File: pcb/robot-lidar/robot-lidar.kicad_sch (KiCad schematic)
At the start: 53 parts, among them J10 Conn_01x18, J11 USB_A, J2 YLIDAR X4, J3 Jack-DC, J5 Conn_01x02, J5 Conn_02x03_Odd_Even, J6 Conn_01x02, J7 Conn_01x02, J7 Conn_ARM_SWD_TagConnect_TC2030, J8 Conn_01x02, J9 Conn_01x18, SW1 SW_SPST, U1 STM32F429VETx, U2 LM317-3.3_SOT-223, U2 MPU-6050, U4 MX1508, U5 MX1508, Y1 Crystal

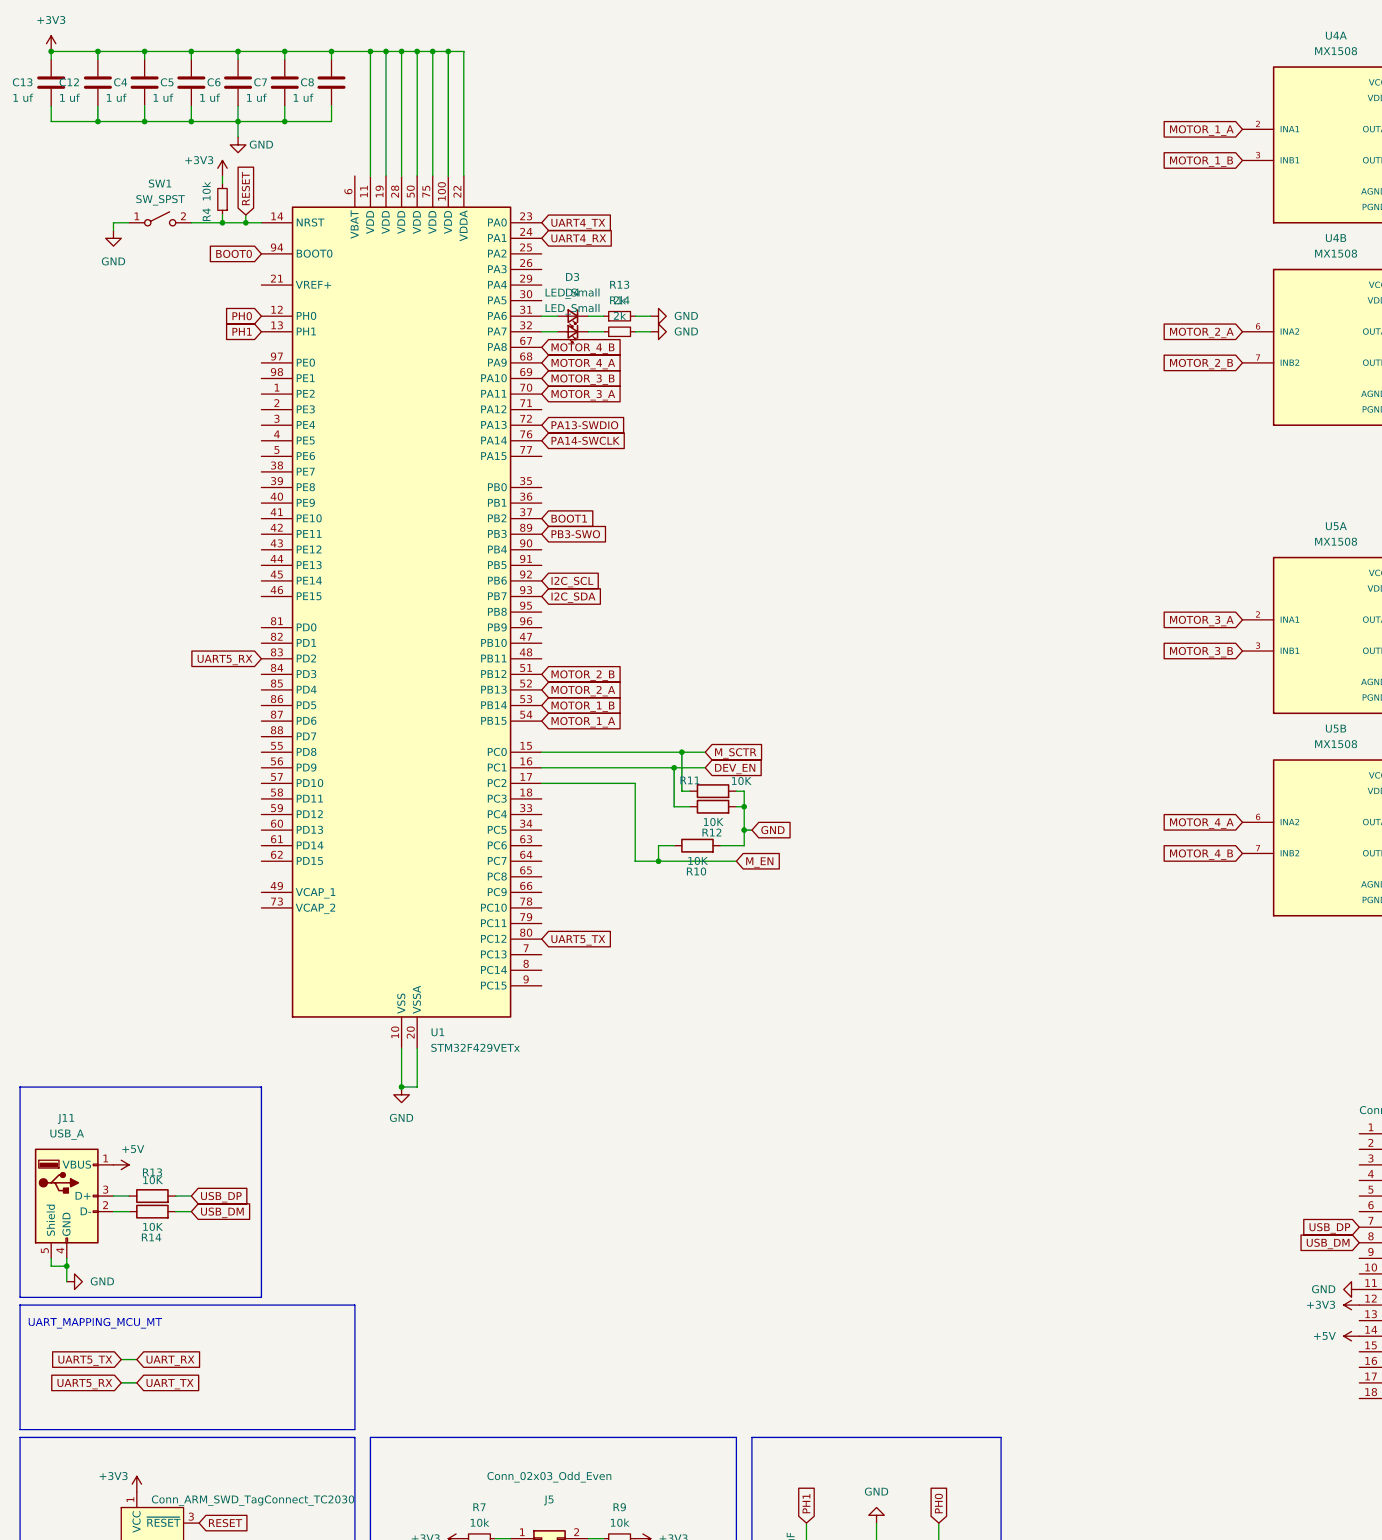
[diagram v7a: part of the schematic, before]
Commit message: stm32f4 to stm32f1 + linkit to raspberry
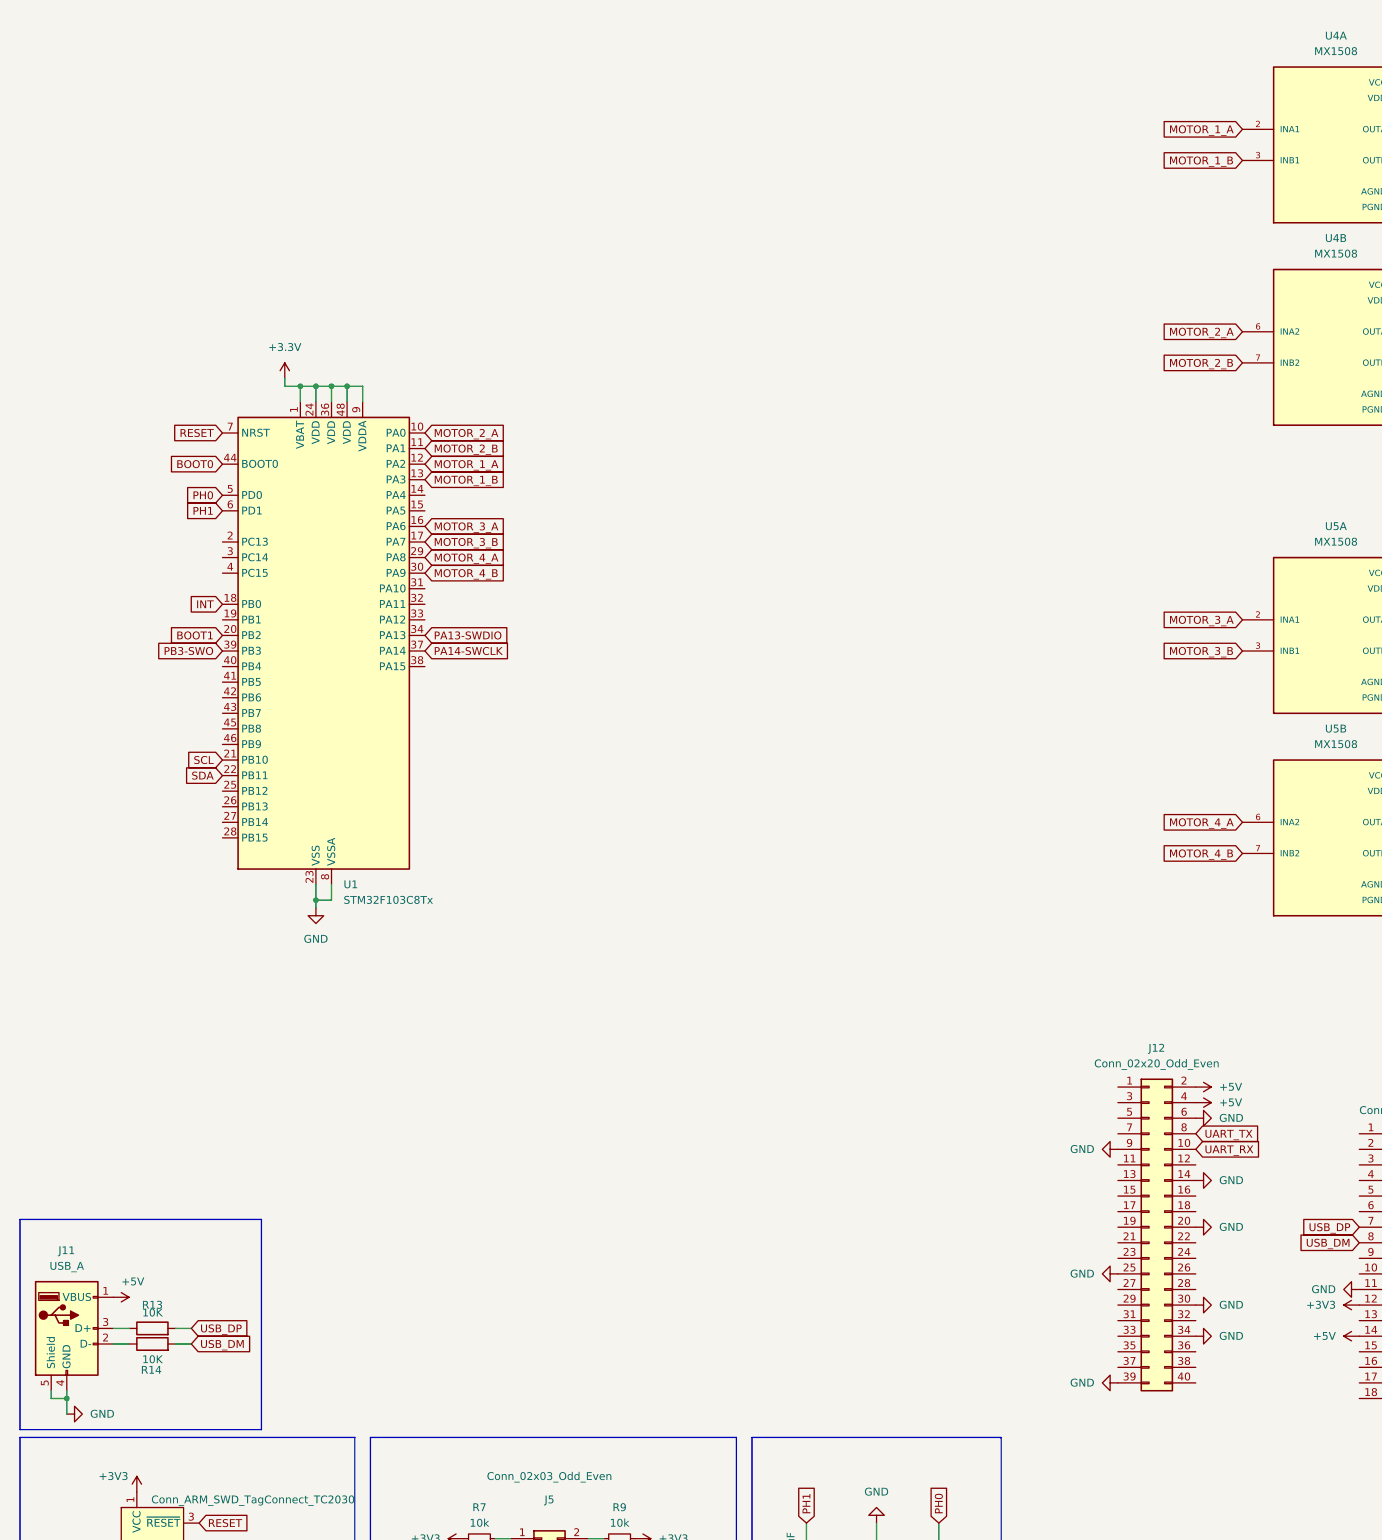
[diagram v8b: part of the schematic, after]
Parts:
- removed C12, C13, C4, C5, C6, C7, C8: 1 uf, Capacitor_SMD:C_0603_1608Metric, symbol Device:C
- removed D3, D4: LED_Small, Resistor_SMD:R_0603_1608Metric, symbol Device:LED_Small
- removed R10, R11, R12: 10K, Resistor_SMD:R_0603_1608Metric, symbol Device:R
- removed R13, R14: 2k, Resistor_SMD:R_0603_1608Metric, symbol Device:R_Small
- removed R4: 10k, Resistor_SMD:R_0603_1608Metric, symbol Device:R_Small
- removed SW1: SW_SPST, Button_Switch_SMD:SW_SPST_CK_RS282G05A3, symbol Switch:SW_SPST
- removed U1: STM32F429VETx, Package_QFP:LQFP-100_14x14mm_P0.5mm, symbol MCU_ST_STM32F4:STM32F429VETx
- added J12: Conn_02x20_Odd_Even, symbol Connector_Generic:Conn_02x20_Odd_Even
- added U1: STM32F103C8Tx, Package_QFP:LQFP-48_7x7mm_P0.5mm, symbol MCU_ST_STM32F1:STM32F103C8Tx
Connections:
- net +5V: now also J12.2 (Pin_2), J12.4 (Pin_4)
- net BOOT0: now also U1.44 (BOOT0)
- net BOOT1: now also U1.20 (PB2)
- net GND: now also J12.14 (Pin_14), J12.20 (Pin_20), J12.25 (Pin_25), J12.30 (Pin_30), J12.34 (Pin_34), J12.39 (Pin_39), J12.6 (Pin_6), J12.9 (Pin_9), U1.23 (VSS), U1.35 (VSS), U1.47 (VSS), U1.8 (VSSA)
- net MOTOR_1_A: now also U1.12 (PA2)
- net MOTOR_1_B: now also U1.13 (PA3)
- net MOTOR_2_A: now also U1.10 (PA0)
- net MOTOR_2_B: now also U1.11 (PA1)
- net MOTOR_3_A: now also U1.16 (PA6)
- net MOTOR_3_B: now also U1.17 (PA7)
- net MOTOR_4_A: now also U1.29 (PA8)
- net MOTOR_4_B: now also U1.30 (PA9)
- net PA13-SWDIO: now also U1.34 (PA13)
- net PA14-SWCLK: now also U1.37 (PA14)
- net PB3-SWO: now also U1.39 (PB3)
- net PH0: now also U1.5 (PD0)
- net PH1: now also U1.6 (PD1)
- net RESET: now also U1.7 (NRST)
- net UART5_RX renamed UART_TX
- net UART_TX: now also J12.8 (Pin_8)
- net UART5_TX renamed UART_RX
- net UART_RX: now also J12.10 (Pin_10)
- new net +3.3V: U1.1 (VBAT), U1.24 (VDD), U1.36 (VDD), U1.48 (VDD), U1.9 (VDDA)
- new net INT: U1.18 (PB0)
- new net SCL: U1.21 (PB10)
- new net SDA: U1.22 (PB11)
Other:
- note removed: "UART_MAPPING_MCU_MT"
- moved on the sheet: J11, R13, R14
